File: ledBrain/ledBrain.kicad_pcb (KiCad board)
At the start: 2 copper layers, 34.2 x 70.7 mm, 26 parts, among them CN1 XT30PW-M, SW2 K2-1112SW-A4SW-04, SW3 K2-1112SW-A4SW-04, U1 QuinLED-ESP32, U2 MT30-F, U3 CH224A, U4 LM2940S-5.0, U5 SN74AHCT32QPWRQ1

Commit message: update
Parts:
- removed C8: 1uF, Capacitor_SMD:C_0603_1608Metric_Pad1.08x0.95mm_HandSolder
- removed C9: 0.1uF, Capacitor_SMD:C_0603_1608Metric_Pad1.08x0.95mm_HandSolder
- removed JP2: SolderJumper_2_Bridged, Jumper:SolderJumper-2_P1.3mm_Bridged_RoundedPad1.0x1.5mm
- removed MIC2: MSM261DGT003, easyeda2kicad:MIC-SMD_6P-L4.0-W2.0_LMD4020T261-OC3
- removed SW3: K2-1112SW-A4SW-04, easyeda2kicad:KEY-TH_K2-1112SW-AXXW-XX
- removed U2: MT30-F, easyeda2kicad:CONN-TH_MT30-M
- added C10: 10uF, Capacitor_SMD:C_0805_2012Metric_Pad1.18x1.45mm_HandSolder, F.Cu at (64.8, 84.4)
- added C11: 100nF, Capacitor_SMD:C_0805_2012Metric_Pad1.18x1.45mm_HandSolder, F.Cu at (64.8, 87.4)
- added C12: 10uF, Capacitor_SMD:C_0805_2012Metric_Pad1.18x1.45mm_HandSolder, F.Cu at (64.8, 90.4)
- added C13: 10uF, Capacitor_SMD:C_0805_2012Metric_Pad1.18x1.45mm_HandSolder, F.Cu at (64.8, 93.5)
- added C14: 10uF, Capacitor_SMD:C_0805_2012Metric_Pad1.18x1.45mm_HandSolder, F.Cu at (64.8, 96.5)
- added C15: 100nF, Capacitor_SMD:C_0805_2012Metric_Pad1.18x1.45mm_HandSolder, F.Cu at (69.7, 78.4)
- added C16: 10uF, Capacitor_SMD:C_0805_2012Metric_Pad1.18x1.45mm_HandSolder, F.Cu at (69.7, 81.4)
- added C17: 10uF, Capacitor_SMD:C_0805_2012Metric_Pad1.18x1.45mm_HandSolder, F.Cu at (69.7, 84.4)
- added C18: 10uF, Capacitor_SMD:C_0805_2012Metric_Pad1.18x1.45mm_HandSolder, F.Cu at (69.7, 87.4)
- added C19: 100nF, Capacitor_SMD:C_0805_2012Metric_Pad1.18x1.45mm_HandSolder, F.Cu at (69.7, 90.4)
- added C20: 15pF, Capacitor_SMD:C_0805_2012Metric_Pad1.18x1.45mm_HandSolder, F.Cu at (69.7, 93.5)
- added C21: 1uF, Capacitor_SMD:C_0805_2012Metric_Pad1.18x1.45mm_HandSolder, F.Cu at (69.7, 96.5)
- added C22: 1uF, Capacitor_SMD:C_0805_2012Metric_Pad1.18x1.45mm_HandSolder, F.Cu at (74.5, 78.4)
- added C23: 0.1uF, Capacitor_SMD:C_0805_2012Metric_Pad1.18x1.45mm_HandSolder, F.Cu at (74.5, 81.4)
- added C24: 0.1uF, Capacitor_SMD:C_0805_2012Metric_Pad1.18x1.45mm_HandSolder, F.Cu at (74.5, 84.4)
- added C25: 0.1uF, Capacitor_SMD:C_0805_2012Metric_Pad1.18x1.45mm_HandSolder, F.Cu at (74.5, 87.4)
- added C26: 2.2uF, Capacitor_SMD:C_0805_2012Metric_Pad1.18x1.45mm_HandSolder, F.Cu at (74.5, 90.4)
- added C27: 0.1uF, Capacitor_SMD:C_0805_2012Metric_Pad1.18x1.45mm_HandSolder, F.Cu at (74.5, 93.5)
- added C28: 0.1uF, Capacitor_SMD:C_0805_2012Metric_Pad1.18x1.45mm_HandSolder, F.Cu at (74.5, 96.5)
- added C29: 1uF, Capacitor_SMD:C_0805_2012Metric_Pad1.18x1.45mm_HandSolder, F.Cu at (79.3, 78.4)
- added C30: 1uF, Capacitor_SMD:C_0805_2012Metric_Pad1.18x1.45mm_HandSolder, F.Cu at (79.3, 81.4)
- added CN5: PJ-328A0-B, easyeda2kicad:AUDIO-TH_PJ-328A0-B, F.Cu at (172.7, 49.5)
- added Cboot1: 1uF, Capacitor_SMD:C_0805_2012Metric_Pad1.18x1.45mm_HandSolder, F.Cu at (79.3, 84.4)
- added Cin1: 10uF, Capacitor_SMD:C_0805_2012Metric_Pad1.18x1.45mm_HandSolder, F.Cu at (79.3, 87.4)
- added Cout1: 10uF, Capacitor_SMD:C_0805_2012Metric_Pad1.18x1.45mm_HandSolder, F.Cu at (79.3, 90.4)
- added JP1: SolderJumper_2_Bridged, Jumper:SolderJumper-2_P1.3mm_Bridged_RoundedPad1.0x1.5mm, F.Cu at (112.0, 65.3)
- added JP3: SolderJumper_2_Bridged, Jumper:SolderJumper-2_P1.3mm_Bridged_RoundedPad1.0x1.5mm, F.Cu at (112.0, 68.8)
- added OSC1: OT2EL4C4JI-111OLP-12.288M, easyeda2kicad:OSC-SMD_4P-L3.2-W2.5-BL, F.Cu at (84.5, 91.3)
- added R10: 10k, Resistor_SMD:R_0603_1608Metric_Pad0.98x0.95mm_HandSolder, F.Cu at (97.4, 76.3)
- added R11: 10k, Resistor_SMD:R_0603_1608Metric_Pad0.98x0.95mm_HandSolder, F.Cu at (97.4, 78.8)
- added R12: 10k, Resistor_SMD:R_0603_1608Metric_Pad0.98x0.95mm_HandSolder, F.Cu at (97.4, 81.3)
- added R13: 100R, Resistor_SMD:R_0603_1608Metric_Pad0.98x0.95mm_HandSolder, F.Cu at (97.4, 83.9)
- added R16: 100R, Resistor_SMD:R_0603_1608Metric_Pad0.98x0.95mm_HandSolder, F.Cu at (97.4, 88.9)
- added R17: 10k, Resistor_SMD:R_0603_1608Metric_Pad0.98x0.95mm_HandSolder, F.Cu at (101.8, 73.8)
- added R18: 10k, Resistor_SMD:R_0603_1608Metric_Pad0.98x0.95mm_HandSolder, F.Cu at (101.8, 76.3)
- added R19: 150k or NC, Resistor_SMD:R_0603_1608Metric_Pad0.98x0.95mm_HandSolder, F.Cu at (101.8, 78.8)
- added R2: 3.3M, Resistor_SMD:R_0603_1608Metric_Pad0.98x0.95mm_HandSolder, F.Cu at (93.1, 73.8)
- added R20: 100k or 0R, Resistor_SMD:R_0603_1608Metric_Pad0.98x0.95mm_HandSolder, F.Cu at (101.8, 81.3)
- added R3: 5.1k, Resistor_SMD:R_0603_1608Metric_Pad0.98x0.95mm_HandSolder, F.Cu at (93.1, 76.3)
- added R4: 1k, Resistor_SMD:R_0603_1608Metric_Pad0.98x0.95mm_HandSolder, F.Cu at (93.1, 78.8)
- added R5: 100R, Resistor_SMD:R_0603_1608Metric_Pad0.98x0.95mm_HandSolder, F.Cu at (93.1, 81.3)
- added R6: 100R, Resistor_SMD:R_0603_1608Metric_Pad0.98x0.95mm_HandSolder, F.Cu at (93.1, 83.9)
- added R7: 10k, Resistor_SMD:R_0603_1608Metric_Pad0.98x0.95mm_HandSolder, F.Cu at (93.1, 86.4)
- added R8: 10k, Resistor_SMD:R_0603_1608Metric_Pad0.98x0.95mm_HandSolder, F.Cu at (93.1, 88.9)
- added R9: 10k, Resistor_SMD:R_0603_1608Metric_Pad0.98x0.95mm_HandSolder, F.Cu at (97.4, 73.8)
- added SW1: EC11E09244BS, easyeda2kicad:SW-TH_EC11XXXXXXXX, F.Cu at (98.0, 63.9)
- added TP1: VDD, TestPoint:TestPoint_Plated_Hole_D3.0mm, F.Cu at (84.7, 79.9)
- added TP2: GND, TestPoint:TestPoint_Plated_Hole_D3.0mm, F.Cu at (84.7, 86.0)
- added U10: HS96L03W2C03, easyeda2kicad:OLED-TH_L27.8-W27.2-P2.54_C9900033791, F.Cu at (76.7, 49.9)
- added U11: MAX9814ETD+T, easyeda2kicad:TDFN-14_L3.0-W3.0-P0.40-BL-EP, F.Cu at (93.0, 92.3)
- added U12: NA-FFA381-A10-1, easyeda2kicad:MIC-SMD_4P-L2.8-W1.9_NA-FFA381-A10-1, F.Cu at (96.7, 92.2)
- added U6: PCM1808PWR, easyeda2kicad:TSSOP-14_L5.0-W4.4-P0.65-LS6.4-BL, F.Cu at (108.4, 59.4)
- added U7: T34069, easyeda2kicad:XFCN_PKT-TH_4P-T34069, F.Cu at (172.5, 39.6)
- added U8: T34069, easyeda2kicad:XFCN_PKT-TH_4P-T34069, F.Cu at (164.0, 39.6)
- added U9: T34069, easyeda2kicad:XFCN_PKT-TH_4P-T34069, F.Cu at (155.5, 39.6)
- C6: value 10uF -> 47pF
- C7: value 10uF -> 100nF
- R15: moved to F.Cu
- U4: value LM2940S-5.0 -> ME3116; footprint easyeda2kicad:SOT-223-3_L6.5-W3.4-P2.30-LS7.0-BR -> easyeda2kicad:SOT-23-6_L2.9-W1.6-P0.95-LS2.8-BL
- moved C7 102.7 mm to (64.8, 81.4)
- moved C6 98.7 mm to (64.8, 78.4)
- moved R15 76.4 mm to (97.4, 86.4)
- moved U4 57.7 mm to (107.7, 65.7), turned to 0 degrees
- moved R14 5.68 mm to (153.4, 31.7)
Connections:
- net IO16/LED1 renamed LED1
- C6 pad 1: VBUS -> +5V
- C6 pad 2: GND -> Net-(U4-FB)
- C7 pad 1: GND -> Net-(U6-VREF)
- C7 pad 2: +5V -> GND
- R14 pad 1: IO33/MAINBUTTON -> MAINBUTTON
- R15 pad 1: IO34/SECOND BUTTON -> +3.3V
- R15 pad 2: +5V -> ROTARY CLK
- SW2 pad 1: IO33/MAINBUTTON -> MAINBUTTON
- U1 pad 18: unconnected-(U1-IO13-Pad18) -> AUDIO SD
- U1 pad 27: unconnected-(U1-IO15-Pad27) -> MAINBUTTON
- U1 pad 3: unconnected-(U1-S_VN-Pad3) -> ROTARY BUTTON
- U1 pad 31: IO32/MIC DATA -> DISPLAY SCL
- U1 pad 32: IO12/MIC CLK -> unconnected-(U1-IO12-Pad32)
- U1 pad 33: unconnected-(U1-IO_4-Pad33) -> DISPLAY SDA
- U1 pad 4: unconnected-(U1-IO35-Pad4) -> AUDIO WS
- U1 pad 5: IO33/MAINBUTTON -> ROTARY DT
- U1 pad 6: IO34/SECOND BUTTON -> ROTARY CLK
- U1 pad 7: unconnected-(U1-IO14-Pad7) -> AUDIO SCK
- U4 pad 1: VBUS -> Net-(U4-BS)
- U4 pad 3: +5V -> Net-(U4-FB)
- U4 pad 4: GND -> Net-(U4-EN)
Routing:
- net +5V: track 85.9 -> 17.1 mm, vias 1 -> 0
- net +3.3V: track 66.2 -> 0.00 mm, vias 1 -> 0
- net IO34/SECOND BUTTON: track 39.1 -> 0.00 mm, vias 1 -> 0
- net LED DATA OUT: track 38.3 -> 0.00 mm
- net IO33/MAINBUTTON: track 33.6 -> 0.00 mm, vias 1 -> 0
- net IO12/MIC CLK: track 29.0 -> 0.00 mm
- net IO32/MIC DATA: track 26.4 -> 0.00 mm
- net Net-(JP2-B): track 4.98 -> 0.00 mm
- net GND: track 13.2 -> 8.79 mm, vias 108 -> 100
- net MAINBUTTON: track 0.00 -> 1.36 mm, vias 0 -> 1
- net VBUS: vias 94 -> 88
- added copper zone on In1.Cu, net GND
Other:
- copper layers 2 -> 4

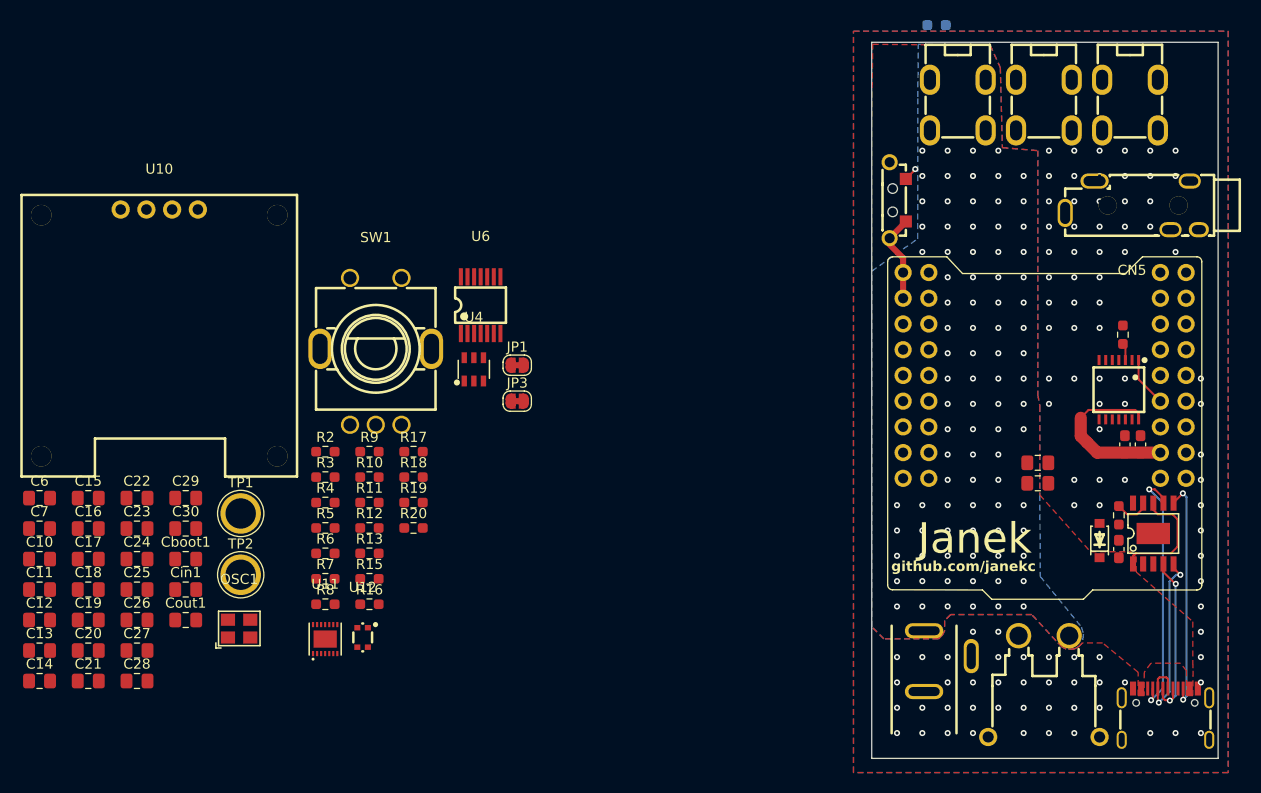
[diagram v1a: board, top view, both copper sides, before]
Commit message: new routing for ledbrain
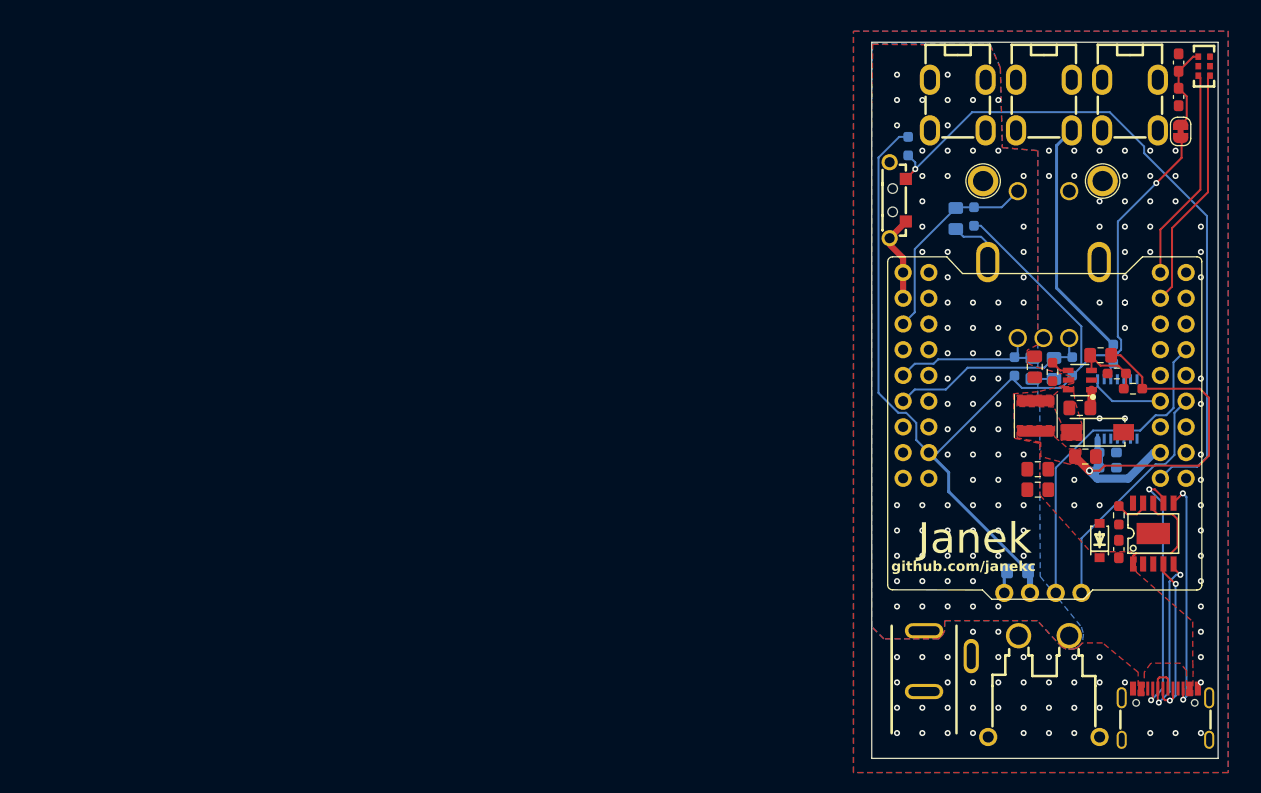
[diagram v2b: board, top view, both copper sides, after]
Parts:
- removed C10, C12, C13, C14, C16, C18: 10uF, Capacitor_SMD:C_0805_2012Metric_Pad1.18x1.45mm_HandSolder
- removed C11, C15, C19: 100nF, Capacitor_SMD:C_0805_2012Metric_Pad1.18x1.45mm_HandSolder
- removed C20: 15pF, Capacitor_SMD:C_0805_2012Metric_Pad1.18x1.45mm_HandSolder
- removed C21, C22, C29, C30: 1uF, Capacitor_SMD:C_0805_2012Metric_Pad1.18x1.45mm_HandSolder
- removed C23, C24: 0.1uF, Capacitor_SMD:C_0805_2012Metric_Pad1.18x1.45mm_HandSolder
- removed C26: 2.2uF, Capacitor_SMD:C_0805_2012Metric_Pad1.18x1.45mm_HandSolder
- removed CN5: PJ-328A0-B, easyeda2kicad:AUDIO-TH_PJ-328A0-B
- removed JP3: SolderJumper_2_Bridged, Jumper:SolderJumper-2_P1.3mm_Bridged_RoundedPad1.0x1.5mm
- removed OSC1: OT2EL4C4JI-111OLP-12.288M, easyeda2kicad:OSC-SMD_4P-L3.2-W2.5-BL
- removed R10, R11, R12, R7, R8, R9: 10k, Resistor_SMD:R_0603_1608Metric_Pad0.98x0.95mm_HandSolder
- removed R13, R16, R5, R6: 100R, Resistor_SMD:R_0603_1608Metric_Pad0.98x0.95mm_HandSolder
- removed R19: 150k or NC, Resistor_SMD:R_0603_1608Metric_Pad0.98x0.95mm_HandSolder
- removed R20: 100k or 0R, Resistor_SMD:R_0603_1608Metric_Pad0.98x0.95mm_HandSolder
- removed U11: MAX9814ETD+T, easyeda2kicad:TDFN-14_L3.0-W3.0-P0.40-BL-EP
- removed U12: NA-FFA381-A10-1, easyeda2kicad:MIC-SMD_4P-L2.8-W1.9_NA-FFA381-A10-1
- removed U6: PCM1808PWR, easyeda2kicad:TSSOP-14_L5.0-W4.4-P0.65-LS6.4-BL
- added C8: 1uF, Capacitor_SMD:C_0603_1608Metric_Pad1.08x0.95mm_HandSolder, F.Cu at (177.3, 38.8)
- added D3: SS54_C123946, easyeda2kicad:SMA_L4.4-W2.8-LS5.4-RD, F.Cu at (169.3, 71.9)
- added L1: 10uH, Inductor_SMD:L_APV_ANR4030, F.Cu at (163.2, 70.3)
- added U2: MSM261DGT003, easyeda2kicad:MIC-SMD_6P-L4.0-W2.0_LMD4020T261-OC3, F.Cu at (179.8, 35.8)
- C1, C17, C2, C25, C27, C28, R1, R15, R17, R18, SW1, U10, U5: moved to B.Cu
- C7: value 100nF -> 0.1uF; footprint Capacitor_SMD:C_0805_2012Metric_Pad1.18x1.45mm_HandSolder -> Capacitor_SMD:C_0603_1608Metric_Pad1.08x0.95mm_HandSolder
- TP1, TP2: footprint TestPoint:TestPoint_Plated_Hole_D3.0mm -> TestPoint:TestPoint_Plated_Hole_D2.0mm
- moved C7 121.5 mm to (177.3, 35.4), turned to -90 degrees
- moved C6 105.7 mm to (169.6, 64.3), turned to 180 degrees
- moved C28 95.7 mm to (165.0, 65.6), turned to -90 degrees
- moved U10 95.1 mm to (163.9, 87.8)
- moved TP2 93.6 mm to (169.8, 47.1)
- moved C27 92.7 mm to (162.9, 65.6), turned to -90 degrees
- moved C17 91.8 mm to (161.4, 85.6), turned to 180 degrees
- moved Cout1 90.3 mm to (168.1, 74.3), turned to 180 degrees
- moved Cboot1 89.5 mm to (167.6, 69.5), turned to 180 degrees
- moved C25 88.7 mm to (155.3, 50.8), turned to -90 degrees
- moved Cin1 86.7 mm to (163.1, 65.5), turned to 90 degrees
- moved TP1 80.3 mm to (158.0, 47.1)
- moved R3 80.2 mm to (172.8, 67.6), turned to 180 degrees
- moved R4 79.2 mm to (171.2, 66.1), turned to 180 degrees
- moved R15 72.5 mm to (166.8, 65.4), turned to 90 degrees
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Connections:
- C7 pad 1: Net-(U6-VREF) -> GND
- C7 pad 2: GND -> Net-(JP1-B)
- R14 pad 2: +5V -> +3.3V
- U1 pad 19: unconnected-(U1-TXD-Pad19) -> MIC DATA
- U1 pad 20: unconnected-(U1-RXD-Pad20) -> MIC CLK
- U8 pad 1: LED DATA OUT -> unconnected-(U8-Pad1)
- U8 pad 3: LED DATA OUT -> unconnected-(U8-Pad3)
- U8 pad 4: LED DATA OUT -> unconnected-(U8-Pad4)
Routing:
- net +3.3V: track 0.00 -> 120.3 mm, vias 0 -> 1
- net MAINBUTTON: track 1.36 -> 68.0 mm
- net DISPLAY SCL: track 0.00 -> 32.7 mm
- net +5V: track 17.1 -> 44.6 mm, vias 0 -> 1
- net LED DATA OUT: track 0.00 -> 24.1 mm
- net MIC CLK: track 0.00 -> 24.0 mm
- net DISPLAY SDA: track 0.00 -> 23.8 mm
- net MIC DATA: track 0.00 -> 21.2 mm
- net ROTARY CLK: track 0.00 -> 20.5 mm
- net ROTARY BUTTON: track 0.00 -> 20.4 mm
- net ROTARY DT: track 0.00 -> 15.7 mm
- net GND: track 8.79 -> 18.8 mm, vias 100 -> 83
- net Net-(JP1-B): track 0.00 -> 8.77 mm
- net Net-(U4-FB): track 0.00 -> 7.45 mm
- net LED1: track 4.95 -> 7.50 mm
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- added copper zone on F.Cu, net +5V
- added copper zone on In2.Cu, net GND
- added copper zone on F.Cu, net Net-(D3-K)
- added copper zone on In2.Cu, net VBUS
